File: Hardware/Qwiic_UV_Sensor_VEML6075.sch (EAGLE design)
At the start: 25 parts, among them J1 GATORGATOR_MINI, J2 GATORGATOR_MINI, J3 GATORGATOR_MINI, J4 GATORGATOR_MINI, J5 GATORGATOR_MINI, J6 GATORGATOR_MINI, J7 GATORGATOR_MINI, J8 GATORGATOR_MINI, U1 VEML6075

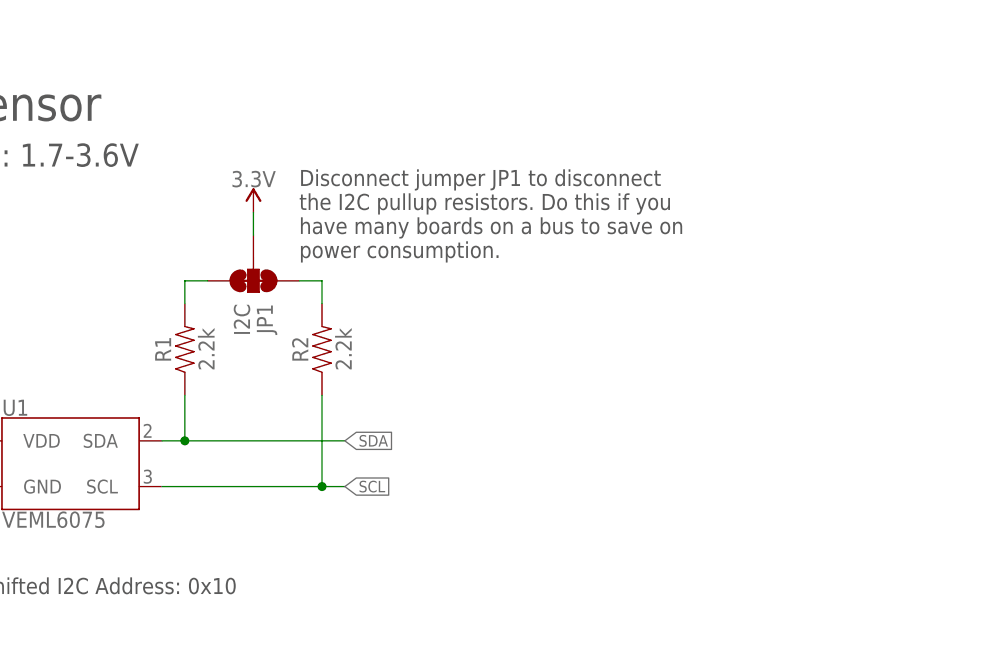
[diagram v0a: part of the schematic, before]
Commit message: adding labelling, removing pullup jumper
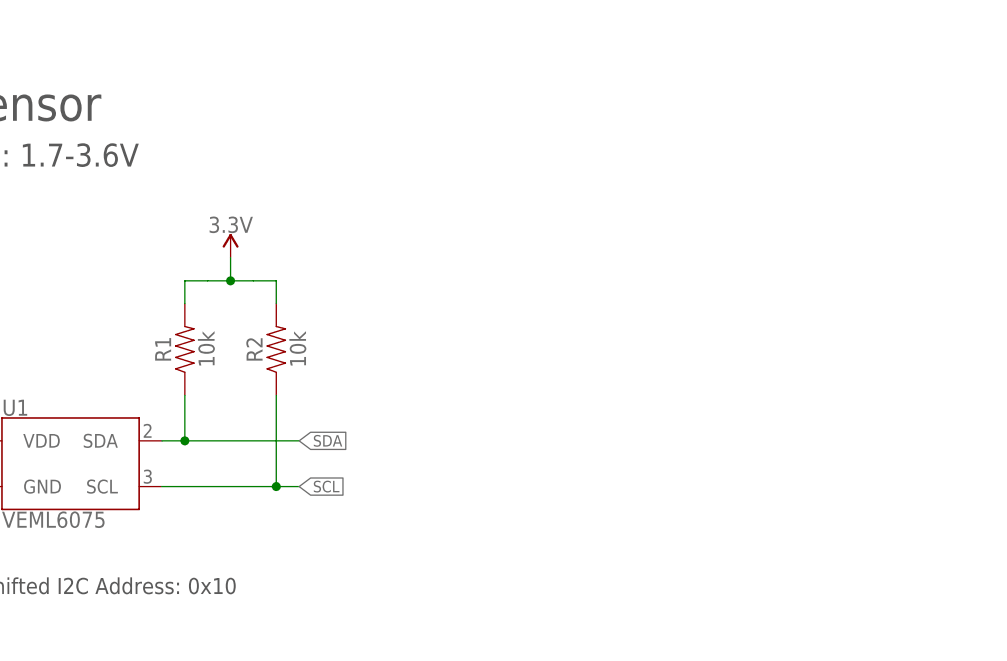
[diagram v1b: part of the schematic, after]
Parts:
- removed JP1: I2C, SparkFun-Jumpers:JUMPER-SMT_3_2-NC_TRACE_SILK
- R1, R2: value 2.2k -> 10k; device SparkFun-Resistors:2.2KOHM-0603-1/10W-1% -> SparkFun-Resistors:10KOHM-0603-1/10W-1%
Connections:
- removed net N$4: JP1.3, R1.2
- removed net N$5: JP1.1, R2.2
- net 3.3V: now also R1.2, R2.2; no longer JP1.2
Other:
- note removed: "Disconnect jumper JP1 to disconnect the I2C pullup resistors. Do this if you have many boards on a bus to save on power consumption."
- moved on the sheet: R2
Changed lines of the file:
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@@
 <?xml version="1.0" encoding="utf-8"?>
 <!DOCTYPE eagle SYSTEM "eagle.dtd">
-<eagle version="9.3.1">
+<eagle version="9.1.0">
 <drawing>
 <settings>
@@
 <part name="SUPPLY1" library="SparkFun-PowerSymbols" deviceset="3.3V" device=""/>
 <part name="GND2" library="SparkFun-PowerSymbols" deviceset="GND" device=""/>
-<part name="R1" library="SparkFun-Resistors" deviceset="2.2KOHM" device="-0603-1/10W-1%" value="2.2k"/>
-<part name="R2" library="SparkFun-Resistors" deviceset="2.2KOHM" device="-0603-1/10W-1%" value="2.2k"/>
-<part name="JP1" library="SparkFun-Jumpers" deviceset="JUMPER-SMT_3_2-NC_TRACE" device="_SILK" value="I2C"/>
+<part name="R1" library="SparkFun-Resistors" deviceset="10KOHM" device="-0603-1/10W-1%" value="10k"/>
+<part name="R2" library="SparkFun-Resistors" deviceset="10KOHM" device="-0603-1/10W-1%" value="10k"/>
 <part name="SUPPLY2" library="SparkFun-PowerSymbols" deviceset="3.3V" device=""/>
 <part name="SUPPLY4" library="SparkFun-PowerSymbols" deviceset="3.3V" device=""/>
@@
 <text x="166.116" y="11.43" size="2.54" layer="94" font="vector">Andy England</text>
 <text x="121.92" y="157.48" size="2.54" layer="97" font="vector">Vin: 1.7-3.6V</text>
-<text x="160.02" y="147.32" size="1.778" layer="97" font="vector">Disconnect jumper JP1 to disconnect
-the I2C pullup resistors. Do this if you
-have many boards on a bus to save on
-power consumption.</text>
 </plain>
 <instances>
@@
 <attribute name="VALUE" x="148.844" y="137.16" size="1.778" layer="96" font="vector" rot="R90" align="top-center"/>
 </instance>
-<instance part="R2" gate="G$1" x="162.56" y="137.16" smashed="yes" rot="R90">
-<attribute name="NAME" x="161.036" y="137.16" size="1.778" layer="95" font="vector" rot="R90" align="bottom-center"/>
-<attribute name="VALUE" x="164.084" y="137.16" size="1.778" layer="96" font="vector" rot="R90" align="top-center"/>
-</instance>
-<instance part="JP1" gate="G$1" x="154.94" y="144.78" smashed="yes" rot="R270">
-<attribute name="NAME" x="155.321" y="142.24" size="1.778" layer="95" font="vector" rot="R270"/>
-<attribute name="VALUE" x="154.559" y="142.24" size="1.778" layer="96" font="vector" rot="R270" align="top-left"/>
-</instance>
-<instance part="SUPPLY2" gate="G$1" x="154.94" y="152.4" smashed="yes">
-<attribute name="VALUE" x="154.94" y="155.194" size="1.778" layer="96" align="bottom-center"/>
+<instance part="R2" gate="G$1" x="157.48" y="137.16" smashed="yes" rot="R90">
+<attribute name="NAME" x="155.956" y="137.16" size="1.778" layer="95" font="vector" rot="R90" align="bottom-center"/>
+<attribute name="VALUE" x="159.004" y="137.16" size="1.778" layer="96" font="vector" rot="R90" align="top-center"/>
+</instance>
+<instance part="SUPPLY2" gate="G$1" x="152.4" y="147.32" smashed="yes">
+<attribute name="VALUE" x="152.4" y="150.114" size="1.778" layer="96" align="bottom-center"/>
 </instance>
 <instance part="SUPPLY4" gate="G$1" x="96.52" y="60.96" smashed="yes">
@@
 </segment>
 <segment>
-<pinref part="JP1" gate="G$1" pin="2"/>
 <pinref part="SUPPLY2" gate="G$1" pin="3.3V"/>
-<wire x1="154.94" y1="149.86" x2="154.94" y2="152.4" width="0.1524" layer="91"/>
+<pinref part="R1" gate="G$1" pin="2"/>
+<wire x1="147.32" y1="142.24" x2="147.32" y2="144.78" width="0.1524" layer="91"/>
+<wire x1="147.32" y1="144.78" x2="149.86" y2="144.78" width="0.1524" layer="91"/>
+<pinref part="R2" gate="G$1" pin="2"/>
+<wire x1="154.94" y1="144.78" x2="157.48" y2="144.78" width="0.1524" layer="91"/>
+<wire x1="157.48" y1="144.78" x2="157.48" y2="142.24" width="0.1524" layer="91"/>
+<wire x1="149.86" y1="144.78" x2="152.4" y2="144.78" width="0.1524" layer="91"/>
+<wire x1="152.4" y1="144.78" x2="154.94" y2="144.78" width="0.1524" layer="91"/>
+<wire x1="152.4" y1="147.32" x2="152.4" y2="144.78" width="0.1524" layer="91"/>
+<junction x="152.4" y="144.78"/>
 </segment>
 <segment>
@@
 <wire x1="144.78" y1="127" x2="147.32" y2="127" width="0.1524" layer="91"/>
 <wire x1="147.32" y1="127" x2="147.32" y2="132.08" width="0.1524" layer="91"/>
-<wire x1="147.32" y1="127" x2="165.1" y2="127" width="0.1524" layer="91"/>
+<wire x1="147.32" y1="127" x2="160.02" y2="127" width="0.1524" layer="91"/>
 <junction x="147.32" y="127"/>
-<label x="165.1" y="127" size="1.27" layer="95" font="vector" xref="yes"/>
+<label x="160.02" y="127" size="1.27" layer="95" font="vector" xref="yes"/>
 </segment>
 <segment>
@@
 <pinref part="U1" gate="G$1" pin="SCL"/>
 <pinref part="R2" gate="G$1" pin="1"/>
-<wire x1="144.78" y1="121.92" x2="162.56" y2="121.92" width="0.1524" layer="91"/>
-<wire x1="162.56" y1="121.92" x2="162.56" y2="132.08" width="0.1524" layer="91"/>
-<wire x1="162.56" y1="121.92" x2="165.1" y2="121.92" width="0.1524" layer="91"/>
-<junction x="162.56" y="121.92"/>
-<label x="165.1" y="121.92" size="1.27" layer="95" font="vector" xref="yes"/>
+<wire x1="144.78" y1="121.92" x2="157.48" y2="121.92" width="0.1524" layer="91"/>
+<wire x1="157.48" y1="121.92" x2="157.48" y2="132.08" width="0.1524" layer="91"/>
+<wire x1="157.48" y1="121.92" x2="160.02" y2="121.92" width="0.1524" layer="91"/>
+<junction x="157.48" y="121.92"/>
+<label x="160.02" y="121.92" size="1.27" layer="95" font="vector" xref="yes"/>
 </segment>
 <segment>
@@
 <label x="119.38" y="58.42" size="1.27" layer="95" font="vector" rot="R180" xref="yes"/>
 <pinref part="J8" gate="G$1" pin="P$1"/>
-</segment>
-</net>
-<net name="N$4" class="0">
-<segment>
-<pinref part="R1" gate="G$1" pin="2"/>
-<pinref part="JP1" gate="G$1" pin="3"/>
-<wire x1="147.32" y1="142.24" x2="147.32" y2="144.78" width="0.1524" layer="91"/>
-<wire x1="147.32" y1="144.78" x2="149.86" y2="144.78" width="0.1524" layer="91"/>
-</segment>
-</net>
-<net name="N$5" class="0">
-<segment>
-<pinref part="JP1" gate="G$1" pin="1"/>
-<pinref part="R2" gate="G$1" pin="2"/>
-<wire x1="160.02" y1="144.78" x2="162.56" y2="144.78" width="0.1524" layer="91"/>
-<wire x1="162.56" y1="144.78" x2="162.56" y2="142.24" width="0.1524" layer="91"/>
 </segment>
 </net>
@@
 </schematic>
 </drawing>
-<compatibility>
-<note version="6.3" minversion="6.2.2" severity="warning">
-Since Version 6.2.2 text objects can contain more than one line,
-which will not be processed correctly with this version.
-</note>
-</compatibility>
 </eagle>

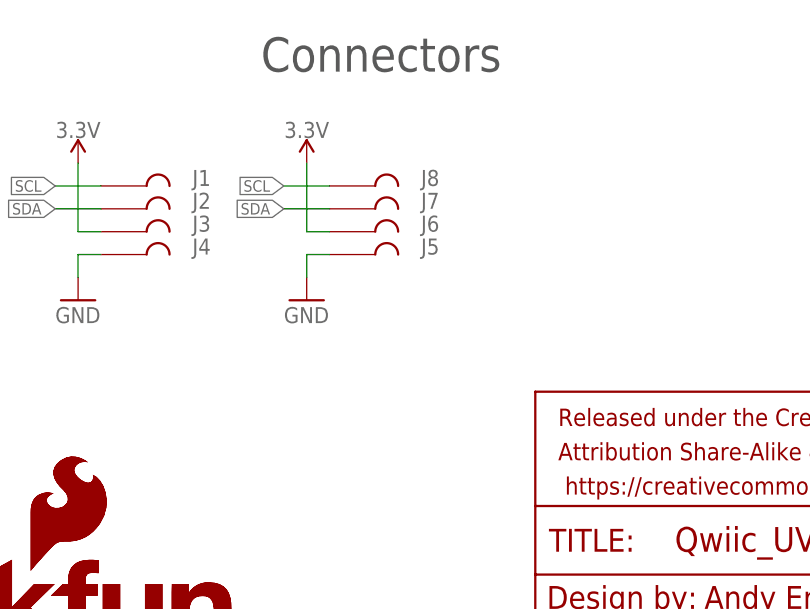
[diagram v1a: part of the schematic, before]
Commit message: adding protection circuitry
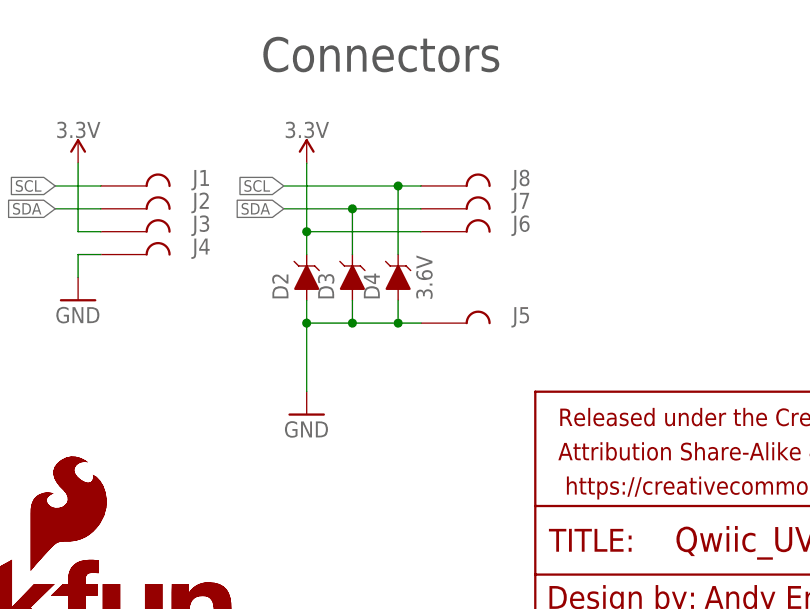
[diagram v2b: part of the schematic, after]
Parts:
- added D2, D3, D4: 3.6V, SparkFun-DiscreteSemi:DIODE-ZENER-BZT52C3V6S
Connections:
- net 3.3V: now also D2.C
- net GND: now also D2.A, D3.A, D4.A
- net SCL: now also D4.C
- net SDA: now also D3.C
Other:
- moved on the sheet: J5, J6, J7, J8
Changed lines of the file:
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@@
 <?xml version="1.0" encoding="utf-8"?>
 <!DOCTYPE eagle SYSTEM "eagle.dtd">
-<eagle version="9.1.0">
+<eagle version="9.3.1">
 <drawing>
 <settings>
@@
 <part name="J7" library="SparkFun-Connectors" deviceset="GATOR" device="GATOR_MINI"/>
 <part name="J8" library="SparkFun-Connectors" deviceset="GATOR" device="GATOR_MINI"/>
+<part name="D2" library="SparkFun-DiscreteSemi" deviceset="DIODE-ZENER" device="-BZT52C3V6S" value="3.6V"/>
+<part name="D3" library="SparkFun-DiscreteSemi" deviceset="DIODE-ZENER" device="-BZT52C3V6S" value="3.6V"/>
+<part name="D4" library="SparkFun-DiscreteSemi" deviceset="DIODE-ZENER" device="-BZT52C3V6S" value="3.6V"/>
 </parts>
 <sheets>
@@
 <attribute name="VALUE" x="121.92" y="63.754" size="1.778" layer="96" align="bottom-center"/>
 </instance>
-<instance part="GND8" gate="1" x="121.92" y="45.72" smashed="yes">
-<attribute name="VALUE" x="119.38" y="43.18" size="1.778" layer="96"/>
+<instance part="GND8" gate="1" x="121.92" y="33.02" smashed="yes">
+<attribute name="VALUE" x="119.38" y="30.48" size="1.778" layer="96"/>
 </instance>
 <instance part="U$2" gate="G$1" x="58.42" y="2.54" smashed="yes"/>
@@
 <attribute name="NAME" x="109.22" y="50.8" size="1.778" layer="95" font="vector"/>
 </instance>
-<instance part="J5" gate="G$1" x="127" y="50.8" smashed="yes">
-<attribute name="NAME" x="134.62" y="50.8" size="1.778" layer="95" font="vector"/>
-</instance>
-<instance part="J6" gate="G$1" x="127" y="53.34" smashed="yes">
-<attribute name="NAME" x="134.62" y="53.34" size="1.778" layer="95" font="vector"/>
-</instance>
-<instance part="J7" gate="G$1" x="127" y="55.88" smashed="yes">
-<attribute name="NAME" x="134.62" y="55.88" size="1.778" layer="95" font="vector"/>
-</instance>
-<instance part="J8" gate="G$1" x="127" y="58.42" smashed="yes">
-<attribute name="NAME" x="134.62" y="58.42" size="1.778" layer="95" font="vector"/>
+<instance part="J5" gate="G$1" x="137.16" y="43.18" smashed="yes">
+<attribute name="NAME" x="144.78" y="43.18" size="1.778" layer="95" font="vector"/>
+</instance>
+<instance part="J6" gate="G$1" x="137.16" y="53.34" smashed="yes">
+<attribute name="NAME" x="144.78" y="53.34" size="1.778" layer="95" font="vector"/>
+</instance>
+<instance part="J7" gate="G$1" x="137.16" y="55.88" smashed="yes">
+<attribute name="NAME" x="144.78" y="55.88" size="1.778" layer="95" font="vector"/>
+</instance>
+<instance part="J8" gate="G$1" x="137.16" y="58.42" smashed="yes">
+<attribute name="NAME" x="144.78" y="58.42" size="1.778" layer="95" font="vector"/>
+</instance>
+<instance part="D2" gate="G$1" x="121.92" y="48.26" smashed="yes" rot="R90">
+<attribute name="NAME" x="119.888" y="45.72" size="1.778" layer="95" font="vector" rot="R90"/>
+</instance>
+<instance part="D3" gate="G$1" x="127" y="48.26" smashed="yes" rot="R90">
+<attribute name="NAME" x="124.968" y="45.72" size="1.778" layer="95" font="vector" rot="R90"/>
+</instance>
+<instance part="D4" gate="G$1" x="132.08" y="48.26" smashed="yes" rot="R90">
+<attribute name="NAME" x="130.048" y="45.72" size="1.778" layer="95" font="vector" rot="R90"/>
+<attribute name="VALUE" x="134.112" y="45.72" size="1.778" layer="96" font="vector" rot="R90" align="top-left"/>
 </instance>
 </instances>
@@
 </segment>
 <segment>
-<wire x1="124.46" y1="53.34" x2="121.92" y2="53.34" width="0.1524" layer="91"/>
+<wire x1="134.62" y1="53.34" x2="121.92" y2="53.34" width="0.1524" layer="91"/>
 <wire x1="121.92" y1="53.34" x2="121.92" y2="60.96" width="0.1524" layer="91"/>
 <pinref part="SUPPLY8" gate="G$1" pin="3.3V"/>
 <pinref part="J6" gate="G$1" pin="P$1"/>
+<pinref part="D2" gate="G$1" pin="C"/>
+<wire x1="121.92" y1="50.8" x2="121.92" y2="53.34" width="0.1524" layer="91"/>
+<junction x="121.92" y="53.34"/>
 </segment>
 </net>
@@
 </segment>
 <segment>
-<wire x1="124.46" y1="50.8" x2="121.92" y2="50.8" width="0.1524" layer="91"/>
-<wire x1="121.92" y1="50.8" x2="121.92" y2="48.26" width="0.1524" layer="91"/>
+<wire x1="134.62" y1="43.18" x2="132.08" y2="43.18" width="0.1524" layer="91"/>
+<wire x1="132.08" y1="43.18" x2="127" y2="43.18" width="0.1524" layer="91"/>
+<wire x1="127" y1="43.18" x2="121.92" y2="43.18" width="0.1524" layer="91"/>
+<wire x1="121.92" y1="43.18" x2="121.92" y2="35.56" width="0.1524" layer="91"/>
 <pinref part="GND8" gate="1" pin="GND"/>
 <pinref part="J5" gate="G$1" pin="P$1"/>
+<pinref part="D2" gate="G$1" pin="A"/>
+<wire x1="121.92" y1="45.72" x2="121.92" y2="43.18" width="0.1524" layer="91"/>
+<junction x="121.92" y="43.18"/>
+<pinref part="D3" gate="G$1" pin="A"/>
+<wire x1="127" y1="45.72" x2="127" y2="43.18" width="0.1524" layer="91"/>
+<junction x="127" y="43.18"/>
+<pinref part="D4" gate="G$1" pin="A"/>
+<wire x1="132.08" y1="45.72" x2="132.08" y2="43.18" width="0.1524" layer="91"/>
+<junction x="132.08" y="43.18"/>
 </segment>
 </net>
@@
 </segment>
 <segment>
-<wire x1="124.46" y1="55.88" x2="119.38" y2="55.88" width="0.1524" layer="91"/>
+<wire x1="134.62" y1="55.88" x2="127" y2="55.88" width="0.1524" layer="91"/>
 <label x="119.38" y="55.88" size="1.27" layer="95" font="vector" rot="R180" xref="yes"/>
 <pinref part="J7" gate="G$1" pin="P$1"/>
+<pinref part="D3" gate="G$1" pin="C"/>
+<wire x1="127" y1="55.88" x2="119.38" y2="55.88" width="0.1524" layer="91"/>
+<wire x1="127" y1="50.8" x2="127" y2="55.88" width="0.1524" layer="91"/>
+<junction x="127" y="55.88"/>
 </segment>
 </net>
@@
 </segment>
 <segment>
-<wire x1="124.46" y1="58.42" x2="119.38" y2="58.42" width="0.1524" layer="91"/>
+<wire x1="134.62" y1="58.42" x2="132.08" y2="58.42" width="0.1524" layer="91"/>
 <label x="119.38" y="58.42" size="1.27" layer="95" font="vector" rot="R180" xref="yes"/>
 <pinref part="J8" gate="G$1" pin="P$1"/>
+<pinref part="D4" gate="G$1" pin="C"/>
+<wire x1="132.08" y1="58.42" x2="119.38" y2="58.42" width="0.1524" layer="91"/>
+<wire x1="132.08" y1="50.8" x2="132.08" y2="58.42" width="0.1524" layer="91"/>
+<junction x="132.08" y="58.42"/>
 </segment>
 </net>

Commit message: post checklist changes
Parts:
- added Q1: 2.5A/30V/105mΩ, SparkFun-DiscreteSemi:MOSFET_PCH-DMG2307L
- added R4: 10k, SparkFun-Resistors:10KOHM-0603-1/10W-1%
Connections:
- new net N$1: J3.P$1, J6.P$1, Q1.D
- new net N$4: D2.A, Q1.G, R4.2
- net 3.3V: now also Q1.S; no longer J3.P$1, J6.P$1
- net GND: now also R4.1; no longer D2.A
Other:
- moved on the sheet: D2, D3, D4, J3, J5, J6, J7, J8

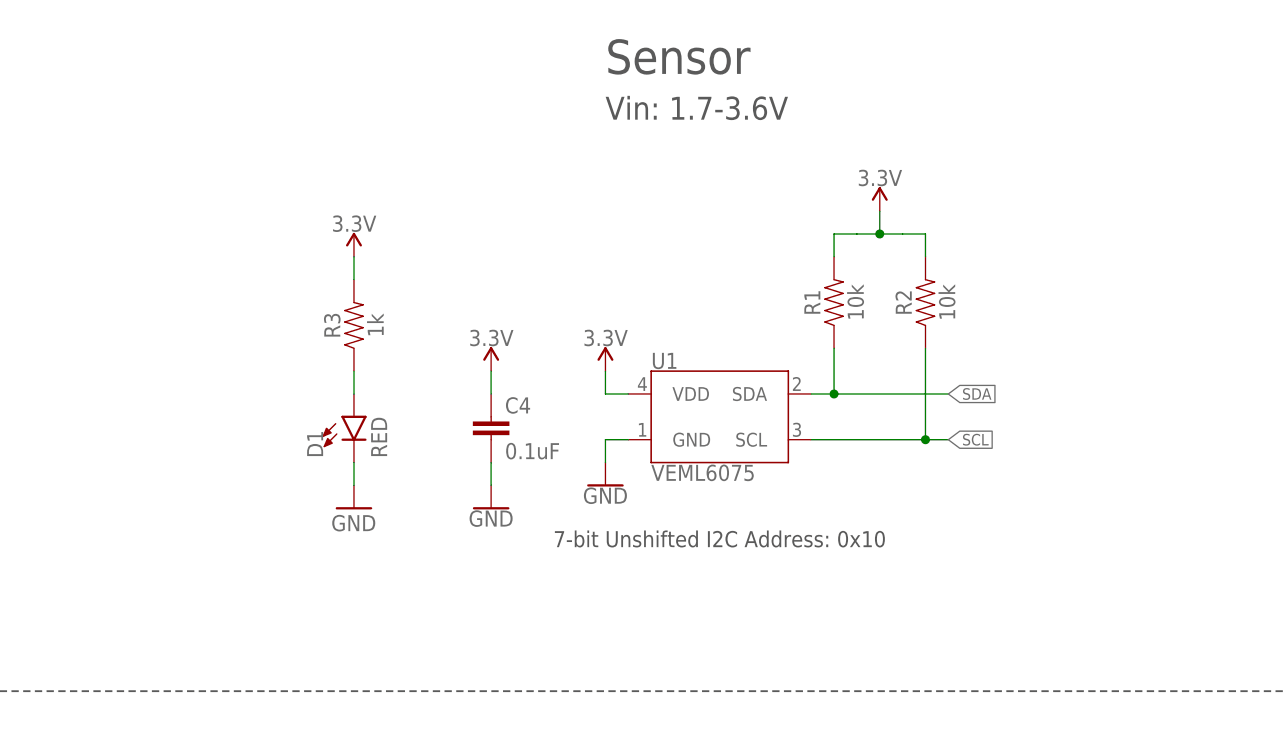
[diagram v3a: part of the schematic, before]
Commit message: updating to VEML6070
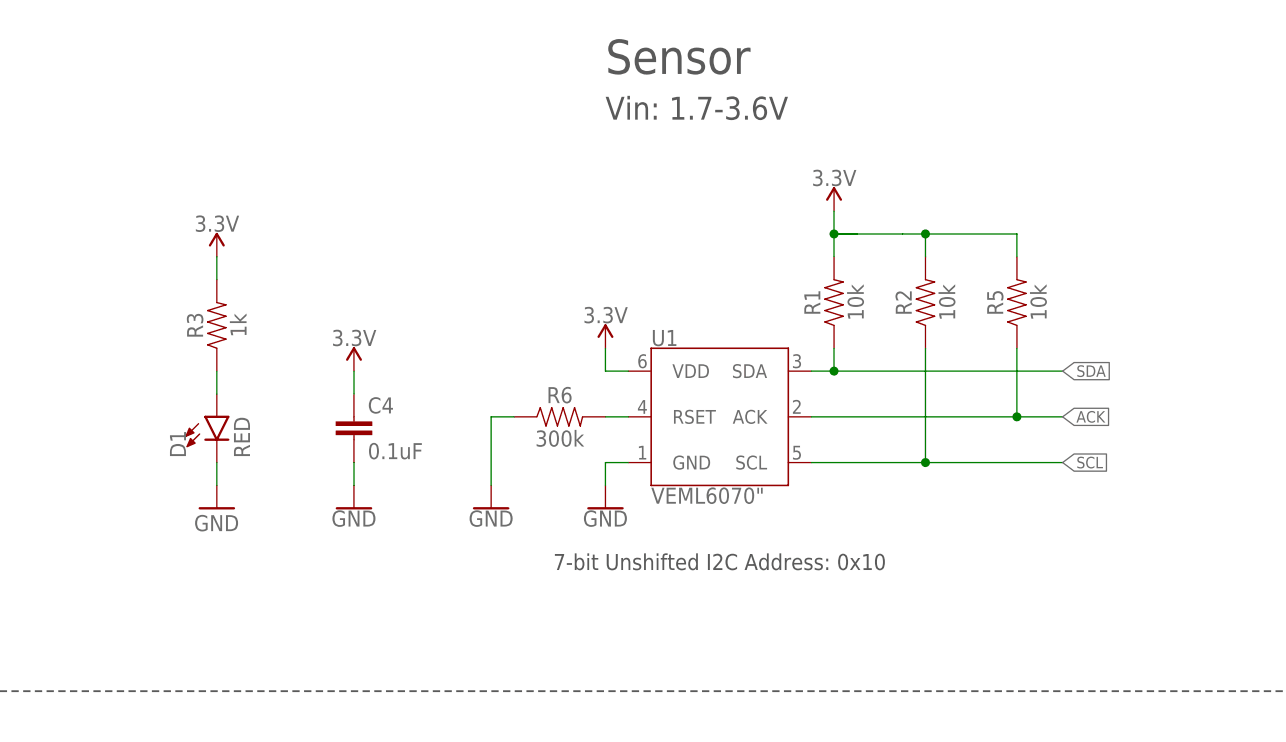
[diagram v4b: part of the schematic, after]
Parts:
- added R5: 10k, SparkFun-Resistors:10KOHM-0603-1/10W-1%
- added R6: 300k, SparkFun-Resistors:300KOHM-0603-1/10W-1%
- U1: value VEML6075 -> VEML6070"; device SparkFun-Sensors:VEML6075 -> SparkFun-Sensors:VEML6070"
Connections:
- new net ACK: R5.1, U1.ACK
- new net N$2: R6.2, U1.RSET
- net 3.3V: now also R5.2
- net GND: now also R6.1
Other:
- moved on the sheet: C4, D1, R3

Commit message: engineer run of checklist
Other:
- note added: "Supply Voltage: 1.7-3.6V"
- note added: "VEML6070 UVA Sensor"
- note added: "v10"
- note removed: "Sensor"
- note removed: "Vin: 1.7-3.6V"
- note removed: "v01"
- moved on the sheet: D2, D3, D4, J1, J2, J3, J4, J5, J6, J7, J8, Q1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
